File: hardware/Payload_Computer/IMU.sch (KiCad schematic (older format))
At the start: 9 parts

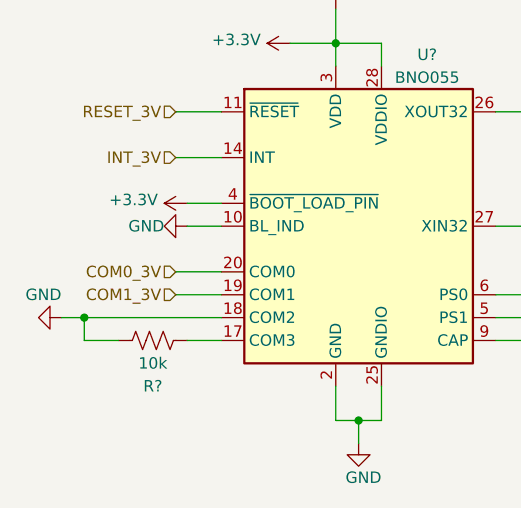
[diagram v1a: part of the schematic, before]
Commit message: Added Barometer, need to find Teensy SPI pin
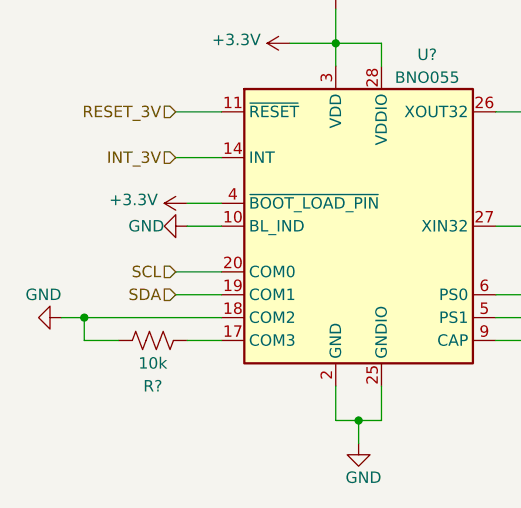
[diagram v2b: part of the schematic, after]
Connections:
- net COM0_3V renamed SCL
- net COM1_3V renamed SDA
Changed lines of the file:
@@
 $Descr A4 11693 8268
 encoding utf-8
-Sheet 11 24
+Sheet 11 27
 Title ""
 Date ""
@@
 INT_3V
 Text HLabel 5150 4050 0    50   Input ~ 0
-COM0_3V
+SCL
 Text HLabel 5150 4150 0    50   Input ~ 0
-COM1_3V
-$Comp
-L power:GND #PWR?
+SDA
+$Comp
+L power:GND #PWR?

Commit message: Minor changes
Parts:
- C?: value 0.1uF -> 1uF
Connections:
- net GND: no longer U?.10 (BL_IND)
- no-connect marks 0 -> 1
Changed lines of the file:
@@
 P 6850 4350
 F 0 "C?" V 7100 4350 50  0000 C CNN
-F 1 "0.1uF" V 7000 4350 50  0000 C CNN
+F 1 "1uF" V 7000 4350 50  0000 C CNN
 F 2 "" H 6888 4200 50  0001 C CNN
 F 3 "~" H 6850 4350 50  0001 C CNN
@@
 	5350 3750 5200 3750
 $Comp
-L power:GND #PWR?
-U 1 1 5FA09E4C
-P 5200 3850
-F 0 "#PWR?" H 5200 3600 50  0001 C CNN
-F 1 "GND" V 5200 3750 50  0000 R CNN
-F 2 "" H 5200 3850 50  0001 C CNN
-F 3 "" H 5200 3850 50  0001 C CNN
-	1    5200 3850
-	0    1    1    0
-$EndComp
-$Comp
 L power:+3.3V #PWR?
 U 1 1 5FA09E52
@@
 Wire Wire Line
 	7950 3600 7950 3850
+NoConn ~ 5200 3850
 $EndSCHEMATC

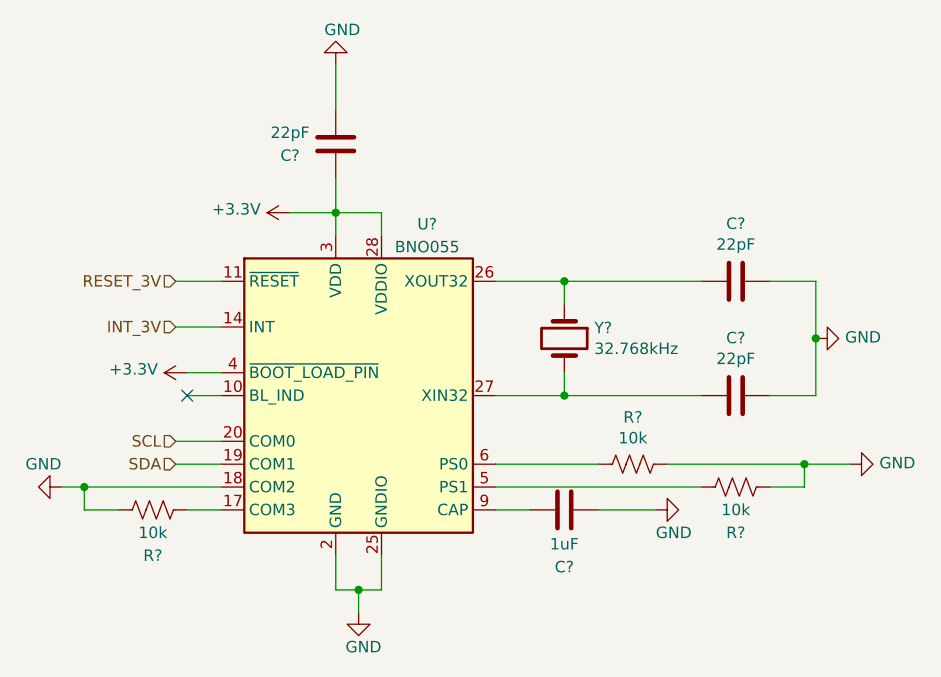
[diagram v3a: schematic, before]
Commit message: Changed CAP values
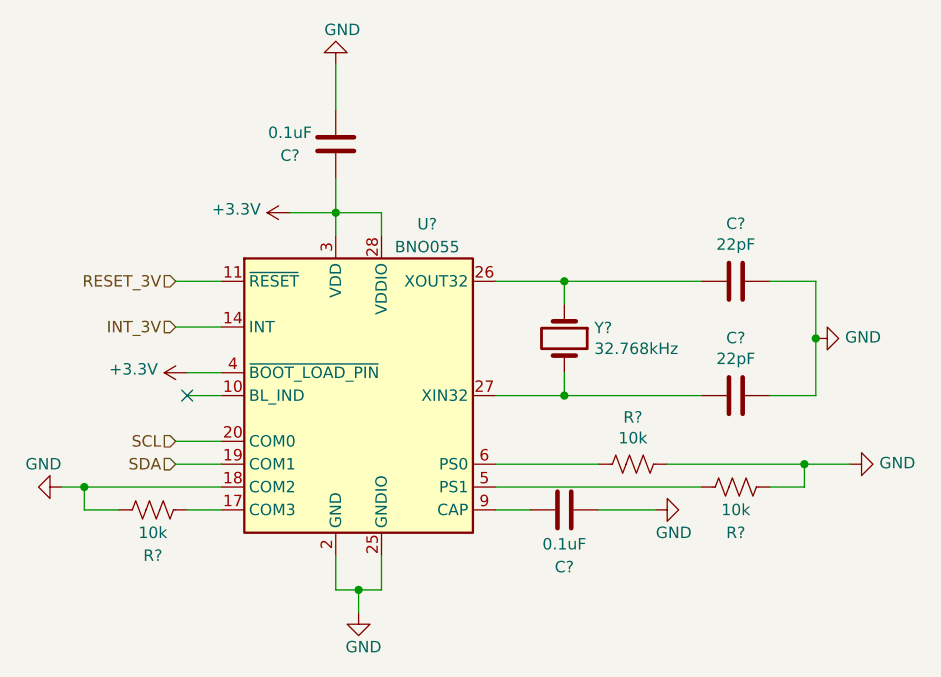
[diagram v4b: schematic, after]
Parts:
- C?: value 1uF -> 0.1uF
- C?: value 22pF -> 0.1uF
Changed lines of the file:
@@
 P 6850 4350
 F 0 "C?" V 7100 4350 50  0000 C CNN
-F 1 "1uF" V 7000 4350 50  0000 C CNN
+F 1 "0.1uF" V 7000 4350 50  0000 C CNN
 F 2 "" H 6888 4200 50  0001 C CNN
 F 3 "~" H 6850 4350 50  0001 C CNN
@@
 P 5850 2750
 F 0 "C?" H 6050 2800 50  0000 C CNN
-F 1 "22pF" H 6050 2700 50  0000 C CNN
+F 1 "0.1uF" H 6050 2700 50  0000 C CNN
 F 2 "" H 5888 2600 50  0001 C CNN
 F 3 "~" H 5850 2750 50  0001 C CNN

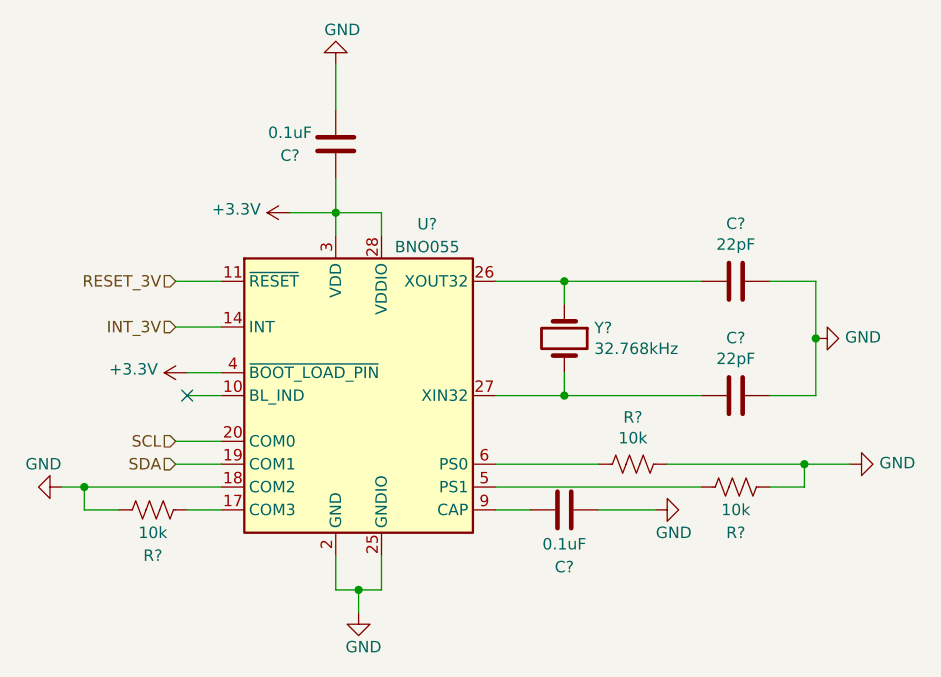
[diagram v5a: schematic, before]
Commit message: Finished Fan Schematic. Working on Servos
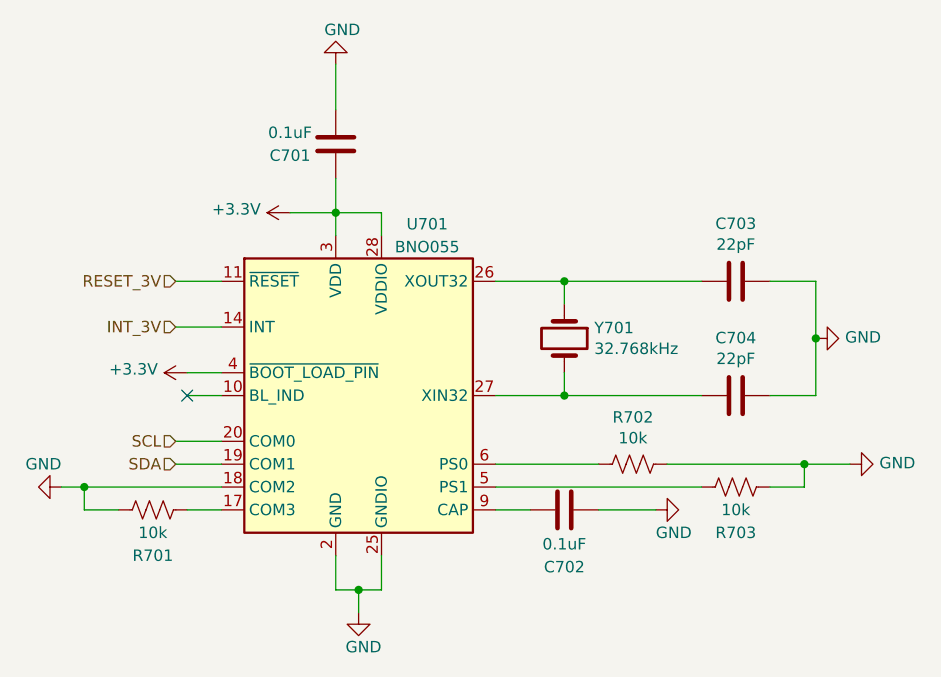
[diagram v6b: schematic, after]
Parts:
- C701, C702, C703, C704: renamed from C?; footprint (none) -> Capacitor_SMD:C_0603_1608Metric_Pad1.08x0.95mm_HandSolder
- R701, R702, R703: renamed from R?; footprint (none) -> Resistor_SMD:R_0603_1608Metric_Pad0.98x0.95mm_HandSolder
- gave numbers to parts that had none: 2
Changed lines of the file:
@@
 $Descr A4 11693 8268
 encoding utf-8
-Sheet 7 26
+Sheet 7 22
 Title ""
 Date ""
@@
 $EndDescr
 $Comp
-L Sensor_Motion:BNO055 U?
+L Sensor_Motion:BNO055 U701
 U 1 1 5FA09DD4
 P 5950 3850
-F 0 "U?" H 6250 4600 50  0000 C CNN
+F 0 "U701" H 6250 4600 50  0000 C CNN
 F 1 "BNO055" H 6250 4500 50  0000 C CNN
 F 2 "Package_LGA:LGA-28_5.2x3.8mm_P0.5mm" H 6200 3200 50  0001 L CNN
@@
 $EndComp
 $Comp
-L power:GND #PWR?
+L power:GND #PWR0707
 U 1 1 5FA09DDC
 P 7950 3600
-F 0 "#PWR?" H 7950 3350 50  0001 C CNN
+F 0 "#PWR0707" H 7950 3350 50  0001 C CNN
 F 1 "GND" V 7955 3472 50  0000 R CNN
 F 2 "" H 7950 3600 50  0001 C CNN
@@
 $EndComp
 $Comp
-L Device:C C?
+L Device:C C703
 U 1 1 5FA09DE3
 P 7600 3350
-F 0 "C?" V 7348 3350 50  0000 C CNN
+F 0 "C703" V 7348 3350 50  0000 C CNN
 F 1 "22pF" V 7439 3350 50  0000 C CNN
-F 2 "" H 7638 3200 50  0001 C CNN
+F 2 "Capacitor_SMD:C_0603_1608Metric_Pad1.08x0.95mm_HandSolder" H 7638 3200 50  0001 C CNN
 F 3 "~" H 7600 3350 50  0001 C CNN
 	1    7600 3350
@@
 $EndComp
 $Comp
-L Device:C C?
+L Device:C C702
 U 1 1 5FA09DE9
 P 6850 4350
-F 0 "C?" V 7100 4350 50  0000 C CNN
+F 0 "C702" V 7100 4350 50  0000 C CNN
 F 1 "0.1uF" V 7000 4350 50  0000 C CNN
-F 2 "" H 6888 4200 50  0001 C CNN
+F 2 "Capacitor_SMD:C_0603_1608Metric_Pad1.08x0.95mm_HandSolder" H 6888 4200 50  0001 C CNN
 F 3 "~" H 6850 4350 50  0001 C CNN
 	1    6850 4350
@@
 	7000 4350 7250 4350
 $Comp
-L Device:R_US R?
+L Device:R_US R702
 U 1 1 5FA09DF4
 P 7150 4150
-F 0 "R?" V 6945 4150 50  0000 C CNN
+F 0 "R702" V 6945 4150 50  0000 C CNN
 F 1 "10k" V 7036 4150 50  0000 C CNN
-F 2 "" V 7190 4140 50  0001 C CNN
+F 2 "Resistor_SMD:R_0603_1608Metric_Pad0.98x0.95mm_HandSolder" V 7190 4140 50  0001 C CNN
 F 3 "~" H 7150 4150 50  0001 C CNN
 	1    7150 4150
@@
 $EndComp
 $Comp
-L Device:R_US R?
+L Device:R_US R703
 U 1 1 5FA09DFA
 P 7600 4250
-F 0 "R?" V 7800 4250 50  0000 C CNN
+F 0 "R703" V 7800 4250 50  0000 C CNN
 F 1 "10k" V 7700 4250 50  0000 C CNN
-F 2 "" V 7640 4240 50  0001 C CNN
+F 2 "Resistor_SMD:R_0603_1608Metric_Pad0.98x0.95mm_HandSolder" V 7640 4240 50  0001 C CNN
 F 3 "~" H 7600 4250 50  0001 C CNN
 	1    7600 4250
@@
 Connection ~ 7900 4150
 $Comp
-L power:GND #PWR?
+L power:GND #PWR0708
 U 1 1 5FA09E07
 P 8100 4150
-F 0 "#PWR?" H 8100 3900 50  0001 C CNN
+F 0 "#PWR0708" H 8100 3900 50  0001 C CNN
 F 1 "GND" V 8105 4022 50  0000 R CNN
 F 2 "" H 8100 4150 50  0001 C CNN
@@
 $EndComp
 $Comp
-L Device:C C?
+L Device:C C704
 U 1 1 5FA09E0D
 P 7600 3850
-F 0 "C?" V 7348 3850 50  0000 C CNN
+F 0 "C704" V 7348 3850 50  0000 C CNN
 F 1 "22pF" V 7439 3850 50  0000 C CNN
-F 2 "" H 7638 3700 50  0001 C CNN
+F 2 "Capacitor_SMD:C_0603_1608Metric_Pad1.08x0.95mm_HandSolder" H 7638 3700 50  0001 C CNN
 F 3 "~" H 7600 3850 50  0001 C CNN
 	1    7600 3850
@@
 	5350 4250 4750 4250
 $Comp
-L power:GND #PWR?
+L power:GND #PWR0701
 U 1 1 5FA09E14
 P 4650 4250
-F 0 "#PWR?" H 4650 4000 50  0001 C CNN
+F 0 "#PWR0701" H 4650 4000 50  0001 C CNN
 F 1 "GND" V 4550 4250 50  0000 R CNN
 F 2 "" H 4650 4250 50  0001 C CNN
@@
 	4750 4250 4650 4250
 $Comp
-L Device:R_US R?
+L Device:R_US R701
 U 1 1 5FA09E1E
 P 5050 4350
-F 0 "R?" V 5250 4350 50  0000 C CNN
+F 0 "R701" V 5250 4350 50  0000 C CNN
 F 1 "10k" V 5150 4350 50  0000 C CNN
-F 2 "" V 5090 4340 50  0001 C CNN
+F 2 "Resistor_SMD:R_0603_1608Metric_Pad0.98x0.95mm_HandSolder" V 5090 4340 50  0001 C CNN
 F 3 "~" H 5050 4350 50  0001 C CNN
 	1    5050 4350
@@
 	4900 4350 4750 4350
 $Comp
-L Device:C C?
+L Device:C C701
 U 1 1 5FA09E25
 P 5850 2750
-F 0 "C?" H 6050 2800 50  0000 C CNN
+F 0 "C701" H 6050 2800 50  0000 C CNN
 F 1 "0.1uF" H 6050 2700 50  0000 C CNN
-F 2 "" H 5888 2600 50  0001 C CNN
+F 2 "Capacitor_SMD:C_0603_1608Metric_Pad1.08x0.95mm_HandSolder" H 5888 2600 50  0001 C CNN
 F 3 "~" H 5850 2750 50  0001 C CNN
 	1    5850 2750
@@
 $EndComp
 $Comp
-L power:GND #PWR?
+L power:GND #PWR0704
 U 1 1 5FA09E2B
 P 5850 2400
-F 0 "#PWR?" H 5850 2150 50  0001 C CNN
+F 0 "#PWR0704" H 5850 2150 50  0001 C CNN
 F 1 "GND" H 5900 2250 50  0000 R CNN
 F 2 "" H 5850 2400 50  0001 C CNN
@@
 	5850 3050 5650 3050
 $Comp
-L power:+3.3V #PWR?
+L power:+3.3V #PWR0703
 U 1 1 5FA09E38
 P 5650 3050
-F 0 "#PWR?" H 5650 2900 50  0001 C CNN
+F 0 "#PWR0703" H 5650 2900 50  0001 C CNN
 F 1 "+3.3V" V 5665 3178 50  0000 L CNN
 F 2 "" H 5650 3050 50  0001 C CNN
@@
 	5950 4700 6050 4700
 $Comp
-L power:GND #PWR?
+L power:GND #PWR0705
 U 1 1 5FA09E44
 P 5950 4800
-F 0 "#PWR?" H 5950 4550 50  0001 C CNN
+F 0 "#PWR0705" H 5950 4550 50  0001 C CNN
 F 1 "GND" H 6050 4650 50  0000 R CNN
 F 2 "" H 5950 4800 50  0001 C CNN
@@
 	5350 3750 5200 3750
 $Comp
-L power:+3.3V #PWR?
+L power:+3.3V #PWR0702
 U 1 1 5FA09E52
 P 5200 3750
-F 0 "#PWR?" H 5200 3600 50  0001 C CNN
+F 0 "#PWR0702" H 5200 3600 50  0001 C CNN
 F 1 "+3.3V" V 5215 3878 50  0000 L CNN
 F 2 "" H 5200 3750 50  0001 C CNN
@@
 SDA
 $Comp
-L power:GND #PWR?
+L power:GND #PWR0706
 U 1 1 5FA09E61
 P 7250 4350
-F 0 "#PWR?" H 7250 4100 50  0001 C CNN
+F 0 "#PWR0706" H 7250 4100 50  0001 C CNN
 F 1 "GND" V 7150 4350 50  0000 R CNN
 F 2 "" H 7250 4350 50  0001 C CNN
@@
 $EndComp
 $Comp
-L Device:Crystal Y?
+L Device:Crystal Y701
 U 1 1 5FA09E67
 P 6850 3600
-F 0 "Y?" V 6804 3731 50  0000 L CNN
+F 0 "Y701" V 6804 3731 50  0000 L CNN
 F 1 "32.768kHz" V 6895 3731 50  0000 L CNN
 F 2 "" H 6850 3600 50  0001 C CNN
